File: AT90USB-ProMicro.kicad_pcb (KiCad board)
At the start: 2 copper layers, 18 x 33 mm, 20 parts, among them J1 Conn_01x12, J2 Conn_01x12, J3 Conn_01x03, U1 AT90USB162-16MU, Y1 8MHz

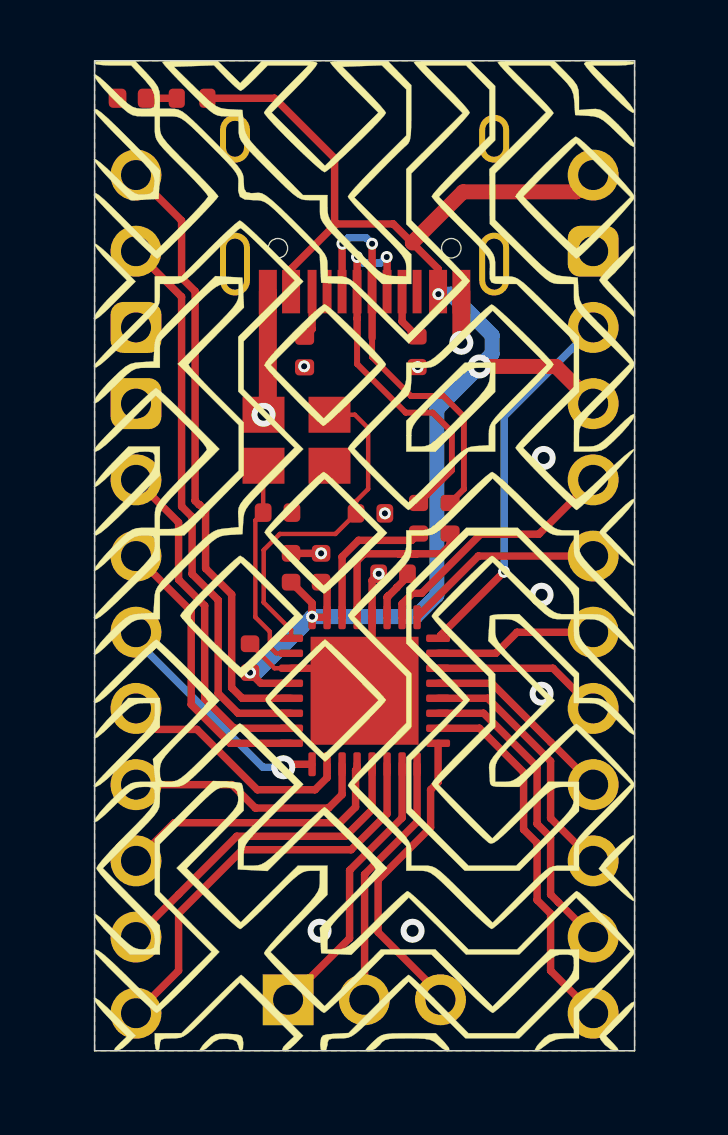
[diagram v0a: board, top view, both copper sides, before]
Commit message: added castellations on all pins
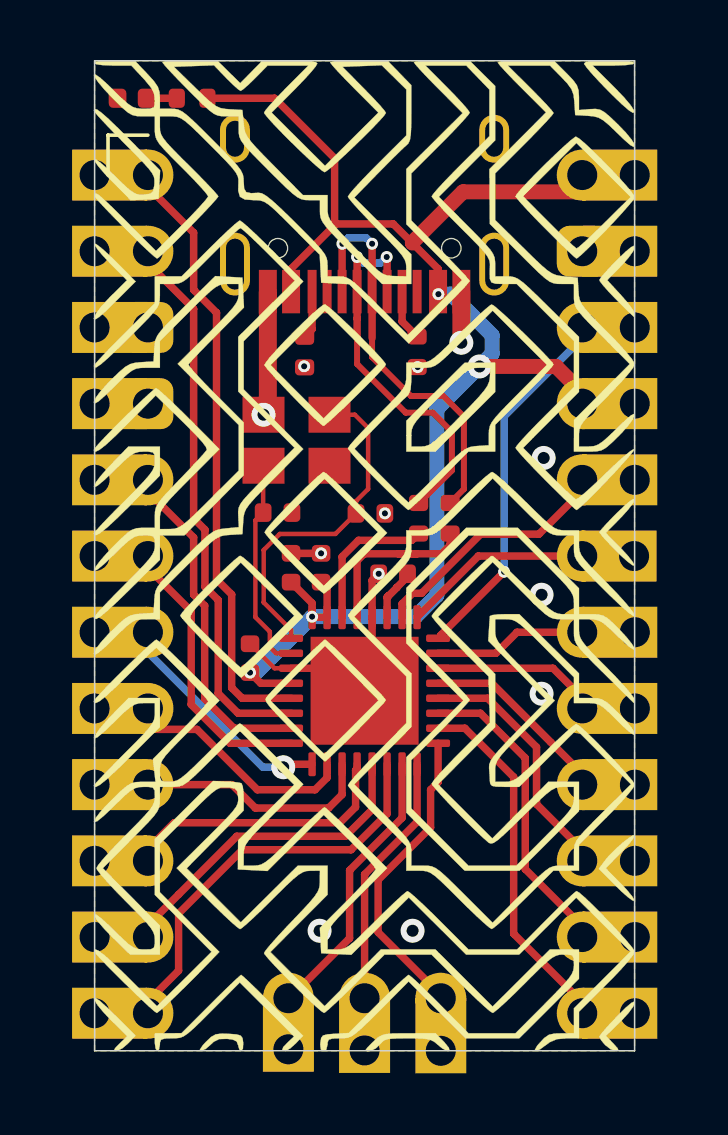
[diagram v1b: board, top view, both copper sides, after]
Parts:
- J1, J3: moved to F.Cu
- moved J1 0.40 mm to (124.8, 64.8), turned to 0 degrees
- moved J2 0.36 mm to (139.3, 64.8)
- moved J3 0.05 mm to (129.5, 92.2), turned to 90 degrees
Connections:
- USB1 pad 3: (no net) -> Net-(USB1-Pad3)
- USB1 pad 9: (no net) -> Net-(USB1-Pad9)

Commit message: correct pin hole placement and castellations
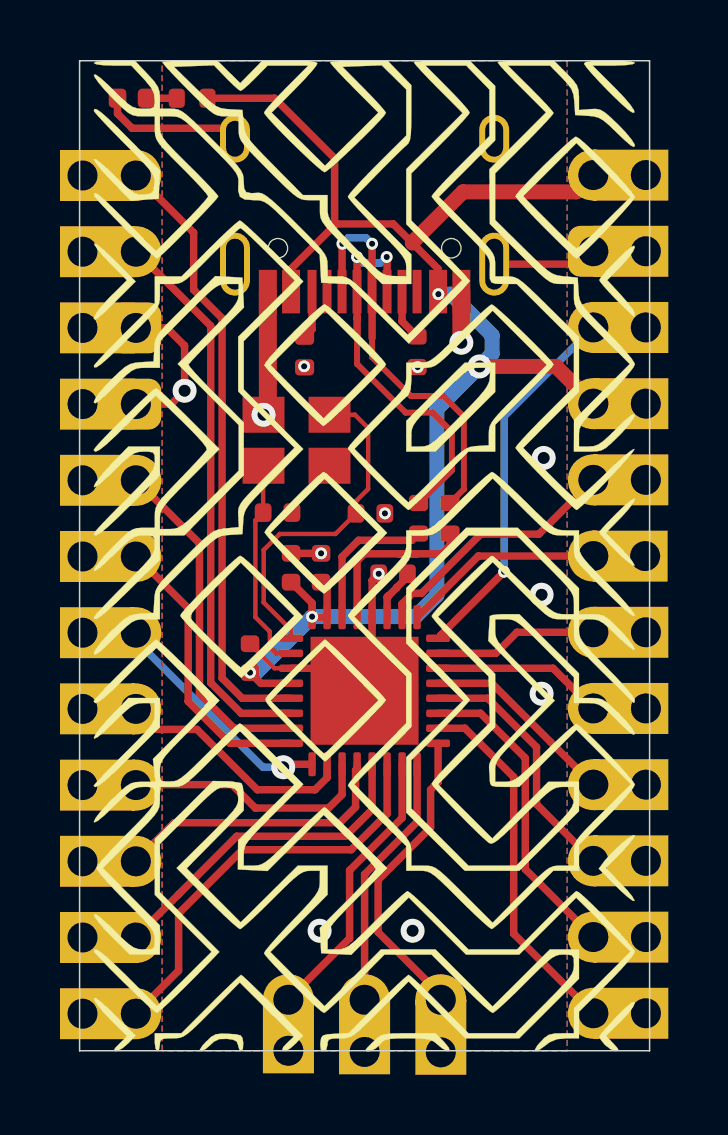
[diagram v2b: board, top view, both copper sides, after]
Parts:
- J1: footprint Connector_PinHeader_2.54mm:PinHeader_1x12_P2.54mm_Vertical -> customheaders:PinHeader_1x12_P2.54mm_Vertical_modified_left
- J2: footprint Connector_PinHeader_2.54mm:PinHeader_1x12_P2.54mm_Vertical -> customheaders:PinHeader_1x12_P2.54mm_Vertical_modified_right
- moved J1 0.40 mm to (124.4, 64.8)
- moved J2 0.37 mm to (139.6, 64.8)
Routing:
- net GND: track 15.4 -> 28.9 mm, vias 12 -> 13
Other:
- board size 18 x 33 mm -> 19 x 33 mm

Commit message: some small tweaks and corrections to mute DRC errors
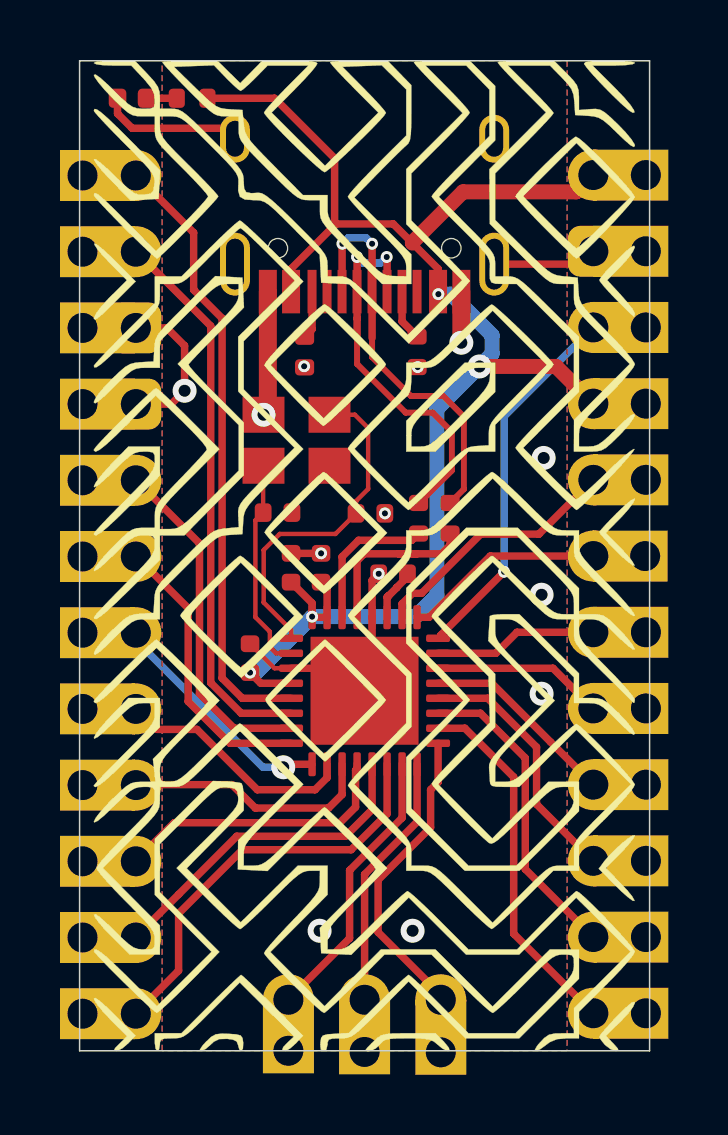
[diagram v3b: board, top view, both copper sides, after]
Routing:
- net GND: track 28.9 -> 32.1 mm
- net PB7: track 6.57 -> 8.17 mm
- net PC7: track 5.73 -> 7.32 mm
- net PC6: track 5.46 -> 7.06 mm
- net PB6: track 8.53 -> 10.1 mm
- net PB5: track 10.4 -> 12.0 mm
- net PB4: track 12.2 -> 13.8 mm
- net PD7: track 11.2 -> 12.8 mm
- net PD6: track 9.51 -> 11.1 mm
- net PD5: track 8.49 -> 10.1 mm
- net PD4: track 8.11 -> 9.71 mm
- net PD3: track 8.00 -> 9.60 mm
- net PD2: track 9.58 -> 11.2 mm
- net PD1: track 11.5 -> 13.1 mm
- net PD0: track 18.5 -> 20.1 mm
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
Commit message: adjusted panel and mousebites
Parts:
- added REF**: Tab, kikit:Tab, F.Cu at (137.4, 60.7)
- added REF**: Tab, kikit:Tab, F.Cu at (126.7, 60.7)
- added REF**: Tab, kikit:Tab, F.Cu at (137.4, 94.2)
- added REF**: Tab, kikit:Tab, F.Cu at (126.7, 94.2)
- J1: footprint customheaders:PinHeader_1x12_P2.54mm_Vertical_modified_left -> customheaders:PinHeader_1x12_P2.54mm_Vertical_modified_right
